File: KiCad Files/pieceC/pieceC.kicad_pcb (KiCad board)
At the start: 2 copper layers, 61.3 x 94.4 mm, 15 parts, among them J1 Conn_01x04_Pin, J2 TC2030-IDC-NL, U1 L7805CV, U2 AMS1117-3.3, U3 TXS0101DCKR, U4 ESP32-WROOM-32E, U5 XT30UPB-M

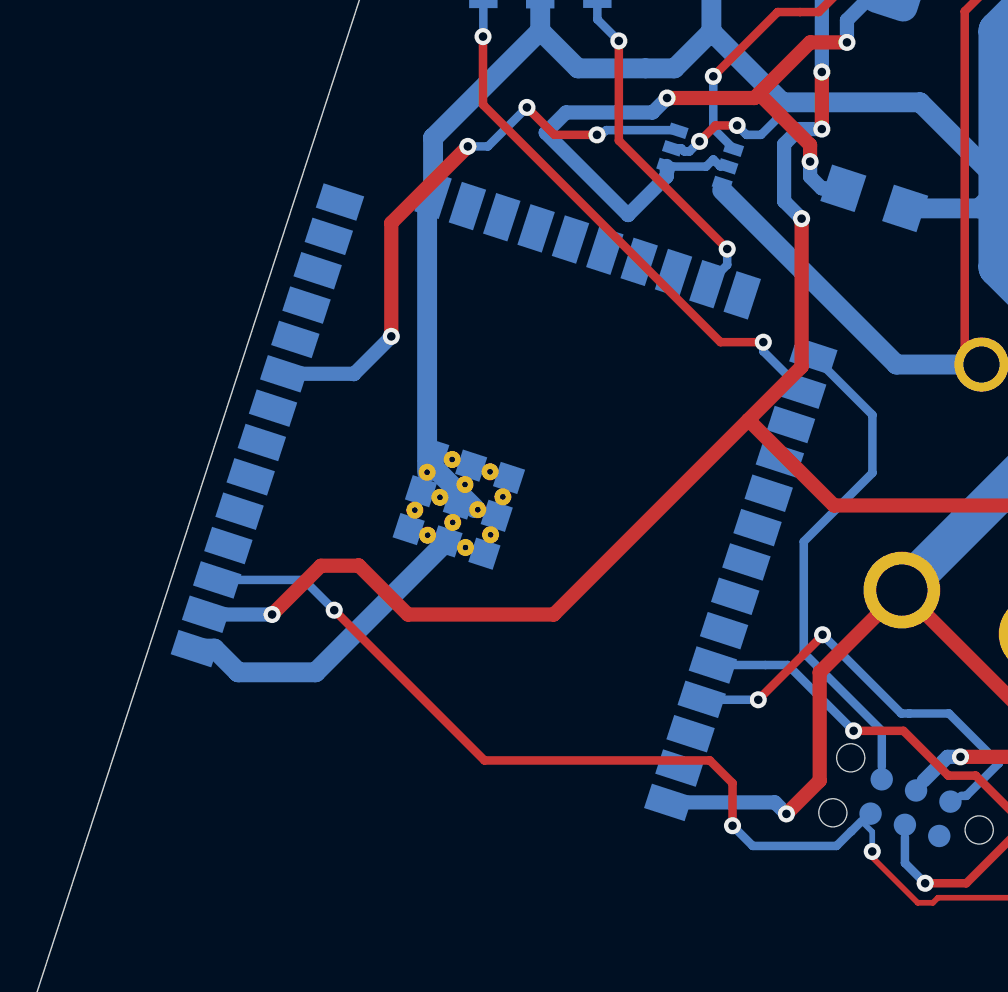
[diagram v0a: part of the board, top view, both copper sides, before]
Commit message: Fixed ESP32 footprint to correct version.
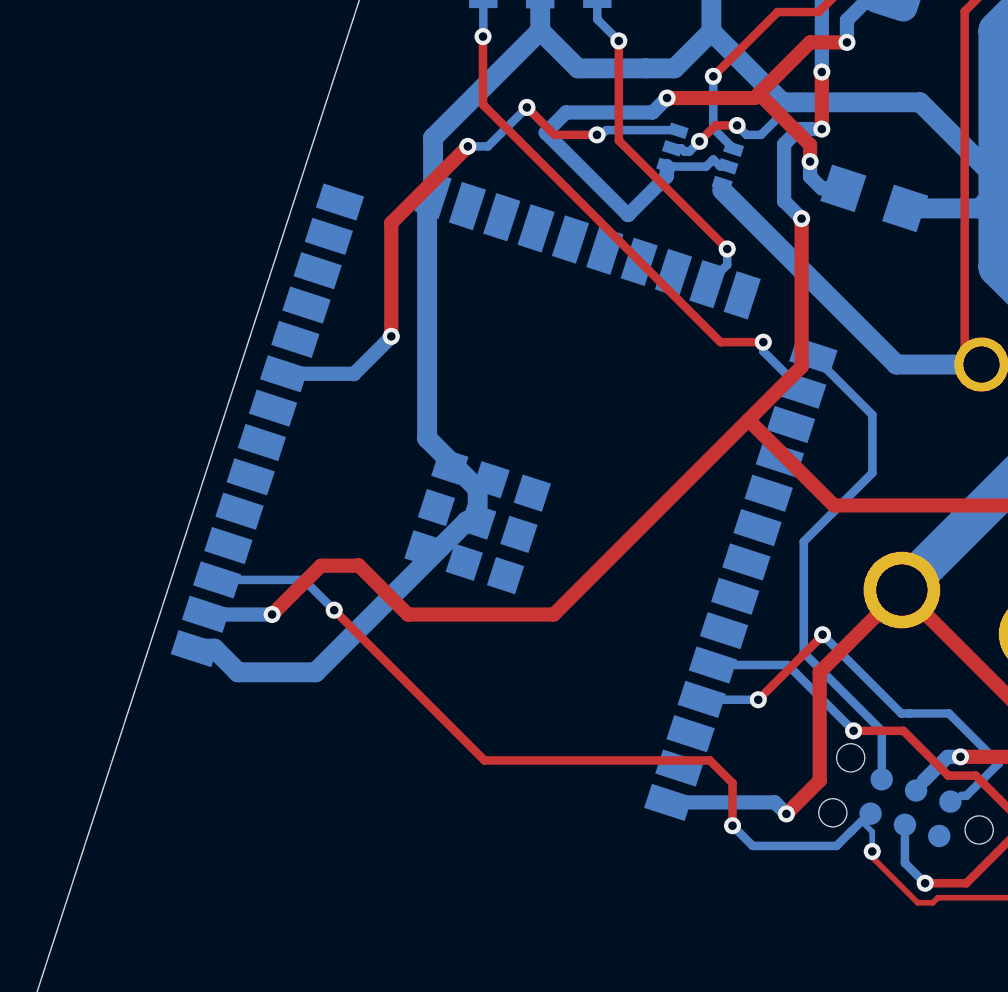
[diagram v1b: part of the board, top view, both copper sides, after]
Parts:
- U4: footprint RF_Module:ESP32-WROOM-32E -> ESP32_WROOM__32_N4:MOD_ESP32-WROOM-32_EXP
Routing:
- net GND: track 144.1 -> 145.9 mm
